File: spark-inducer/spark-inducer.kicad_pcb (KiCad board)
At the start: 2 copper layers, 233.3 x 128.5 mm, 105 parts, among them J1 Eurorack_Power_Header, J10 IO_A_1, J11 IO_A_3, J12 IO_A_2, J13 IO_A_4, J14 IO_B_1, J15 IO_B_3, J16 IO_B_2, J17 IO_B_4, J18 REF_SELECT, J19 POWER_A_1, J2 IO1, J20 POWER_A_2, J21 POWER_A_3, J22 POWER_A_4, J23 POWER_B_1, J24 POWER_B_2, J25 POWER_B_3, J26 POWER_B_4, J3 IO2, J4 IO3, J5 IO4, J6 IO5, J7 IO6, J8 OUT1, J9 OUT2, SW1 SWITCH, U1 TL072B, U2 TL072B, U3 TL431B, U4 L78LXX, U5 LM4040, U6 REF50XX

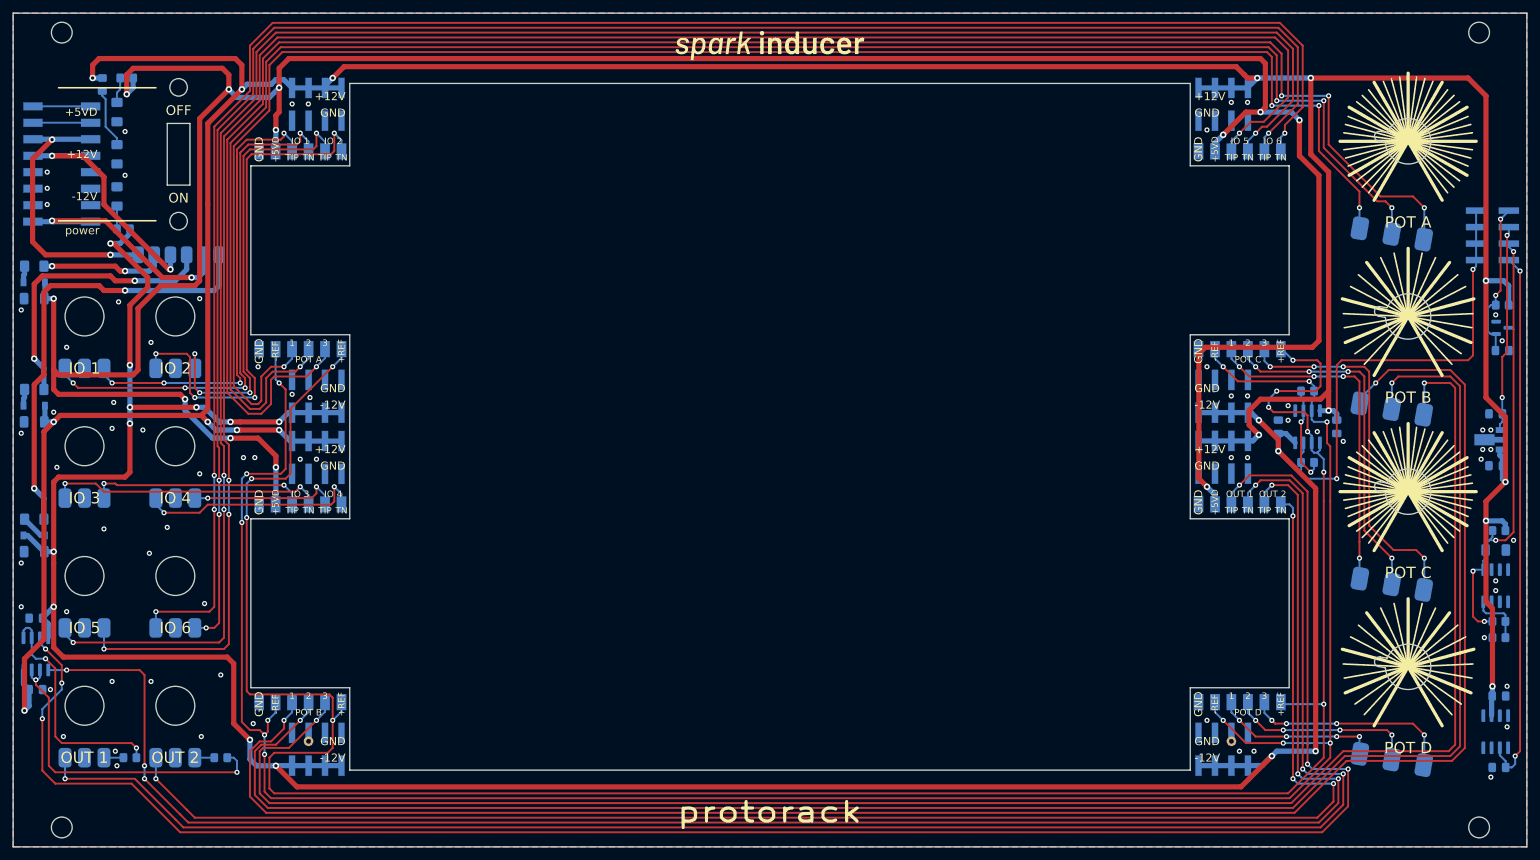
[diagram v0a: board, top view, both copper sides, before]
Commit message: Add ground clip attachment point, test points, rubber feet
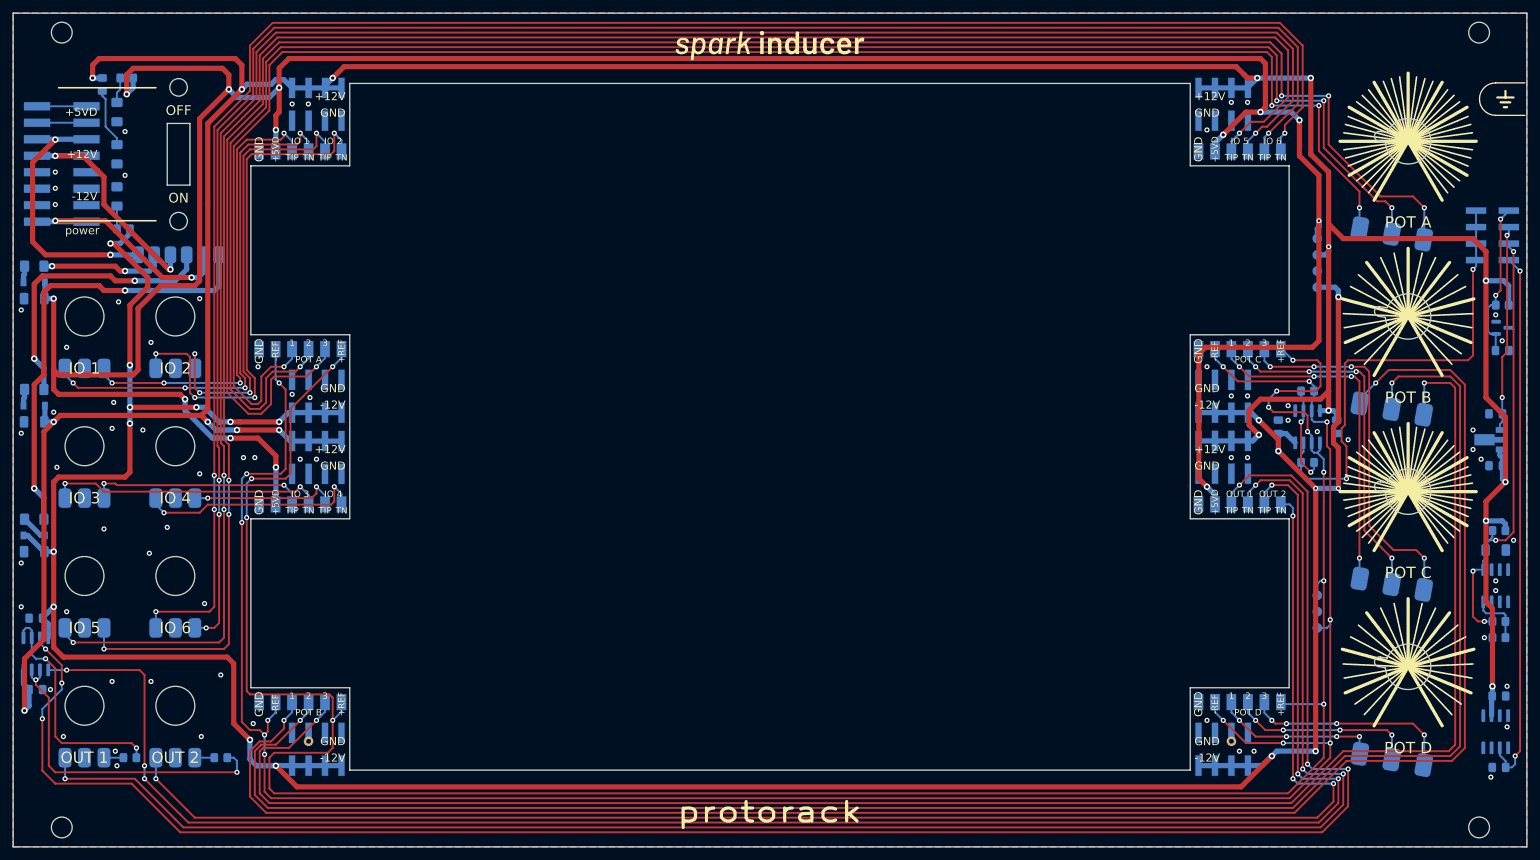
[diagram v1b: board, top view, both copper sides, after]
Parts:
- added H29: FOOT_TL, Protorack:3M_SJ-5023, F.Cu at (74.8, 58.2)
- added H30: FOOT_BL, Protorack:3M_SJ-5023, F.Cu at (74.8, 146.8)
- added H31: FOOT_TR, Protorack:3M_SJ-5023, F.Cu at (219.8, 58.2)
- added H32: FOOT_BR, Protorack:3M_SJ-5023, F.Cu at (219.8, 146.8)
- added TP3: +5V, TestPoint:TestPoint_Pad_D1.5mm, B.Cu at (231.7, 73.5)
- added TP4: +12V, TestPoint:TestPoint_Pad_D1.5mm, B.Cu at (231.7, 76.0)
- added TP5: GND, TestPoint:TestPoint_Pad_D1.5mm, B.Cu at (231.7, 78.5)
- added TP6: -12V, TestPoint:TestPoint_Pad_D1.5mm, B.Cu at (231.7, 81.0)
- added TP7: +REF, TestPoint:TestPoint_Pad_D1.5mm, B.Cu at (231.7, 128.5)
- added TP8: GND, TestPoint:TestPoint_Pad_D1.5mm, B.Cu at (231.7, 131.0)
- added TP9: -REF, TestPoint:TestPoint_Pad_D1.5mm, B.Cu at (231.7, 133.5)
- D1, D2, D3: footprint LED_SMD:LED_1206_3216Metric_Pad1.42x1.75mm_HandSolder -> Protorack:LED_1206_3216Metric_ReverseMount_HandSolder
- D4, D5, D6: footprint Diode_SMD:D_SOD-123 -> Protorack:D_SOD-123
- H1, H2: footprint Protorack:Screw_ISO4762_M2x6 -> Protorack:Screw_ISO7380_M2-5x6
- U4: value L78LXX -> L78Lxx; footprint Package_TO_SOT_SMD:SOT-89-3 -> Protorack:SOT-89-3_ThermalReliefs
- U6: value REF50XX -> REF50xx
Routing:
- net -12V: track 432.2 -> 470.3 mm, vias 15 -> 18
- net +12V: track 594.8 -> 571.4 mm, vias 16 -> 17
- net /-REF: track 349.6 -> 352.6 mm, vias 12 -> 13
- net /+REF: track 356.3 -> 359.3 mm, vias 10 -> 11
- net +5V: track 433.9 -> 436.7 mm, vias 12 -> 13
- net /-12V_IN: track 39.0 -> 37.1 mm
- net /+12V_IN: track 39.2 -> 37.4 mm
- net /+5V_IN: track 43.0 -> 41.9 mm
- net /+REF_UNBUF: track 72.4 -> 73.3 mm
- net GND: vias 71 -> 69
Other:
- board text added: "2022 Rev.3"
- board text added: "L78Lxx"
- board text added: "PROBE GND"
- board text added: "REF50xx"
- board text removed: "2022 Rev.2"
- board text removed: "L78LXX"
- board text removed: "REF50XX"

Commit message: Update files to KiCad 7, Fix edge clearance, Add more spokes to washers
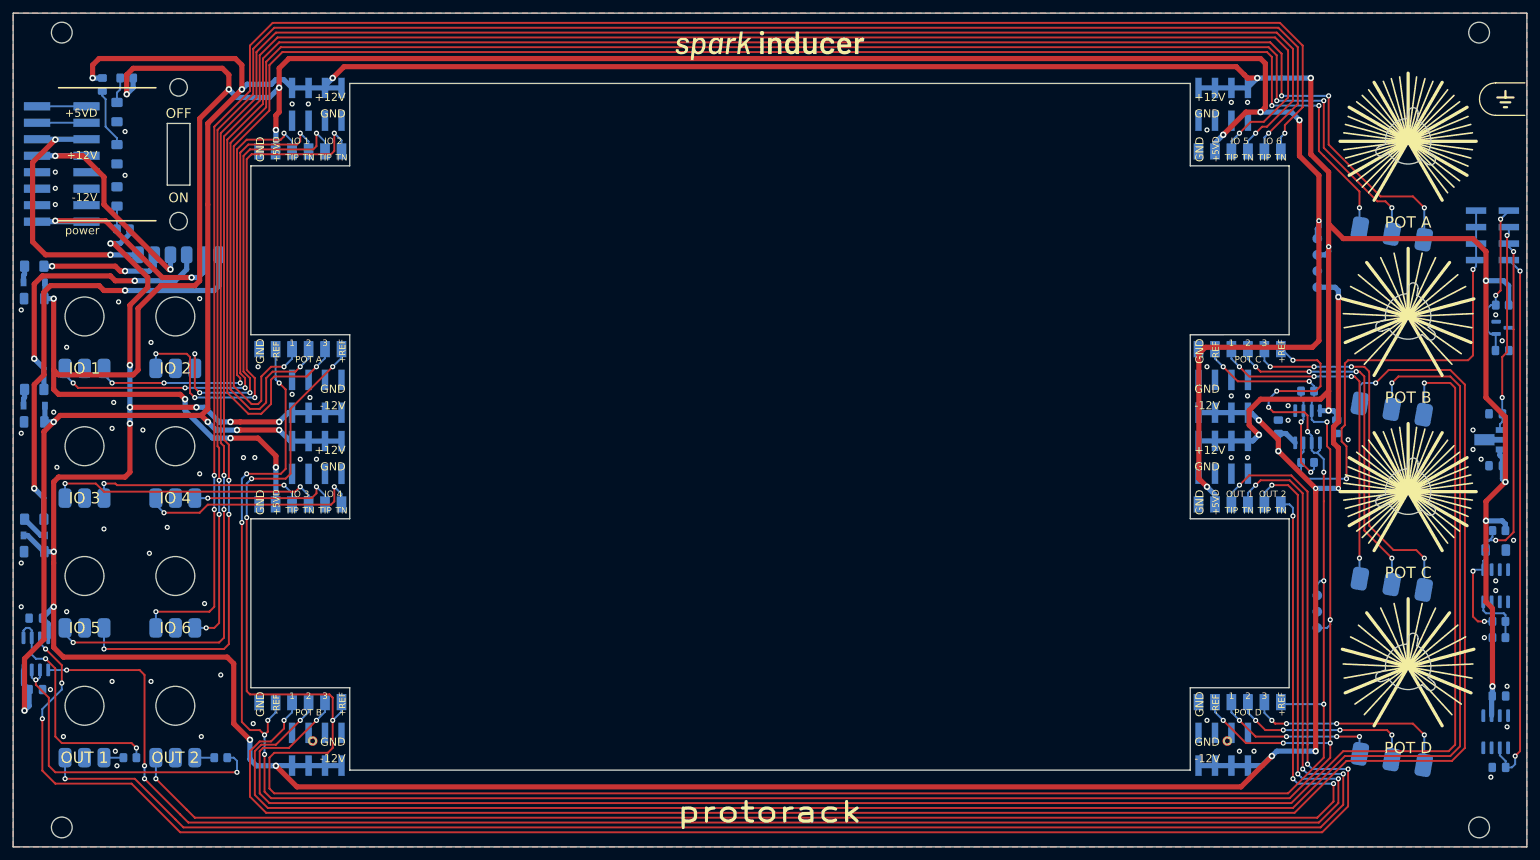
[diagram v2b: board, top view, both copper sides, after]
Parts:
- F1: value 1206L020 -> 200mA
- F2, F3: value 1206L020 -> 100mA
- U1, U2: value TL072B -> TL072H
- moved TP1 0.64 mm to (76.9, 150.9), turned to 90 degrees
- moved TP2 0.64 mm to (217.8, 150.9)
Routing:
- net /POT_B_1: track 286.4 -> 287.6 mm
